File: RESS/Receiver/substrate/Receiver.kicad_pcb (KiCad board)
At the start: 2 copper layers, 94 x 71.1 mm, 19 parts, among them J3 ADP_L, J4 ADP_R, J5 Power, J6 RESS_OUT1, SW1 SW_SPDT, SW2 SW_DIP_x02, U1 LTV-817, U2 RR-1A, U3 TA48033S, U4 TC74HC32AP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

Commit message: P10を3.3Vと接続するのを忘れていたので修正
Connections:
- J4 pad 5: (no net) -> +3V3
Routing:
- net +3V3: track 55.6 -> 65.1 mm

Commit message: 送信基板の追加とファイルの整理
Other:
- board text added: "JLCJLCJLCJLC"

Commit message: 回路の細かな修正
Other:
- board text added: "RESS-Receiver 2022 Ichinoseki-B"
- board text removed: "RESS-Receiver 2022 Ichinoseki-B Falco"

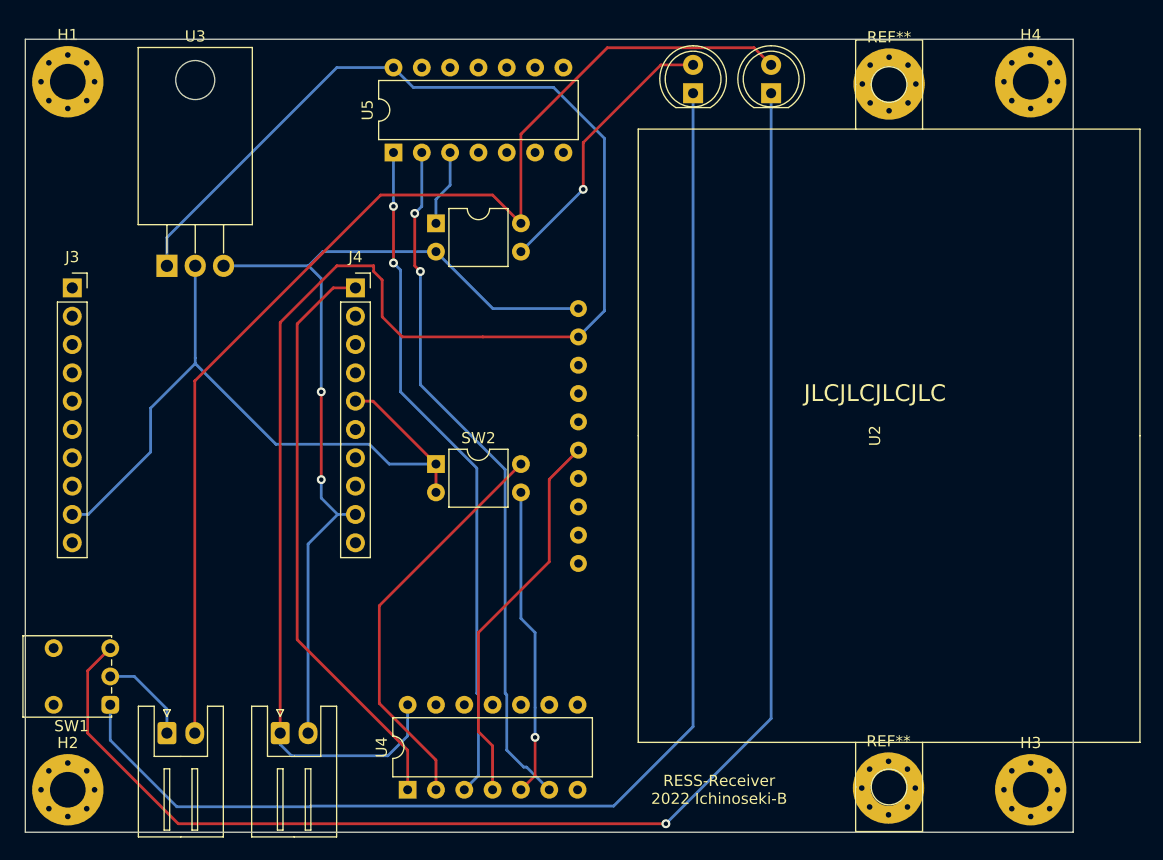
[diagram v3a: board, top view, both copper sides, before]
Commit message: 基板が燃えるほどのミスを修正
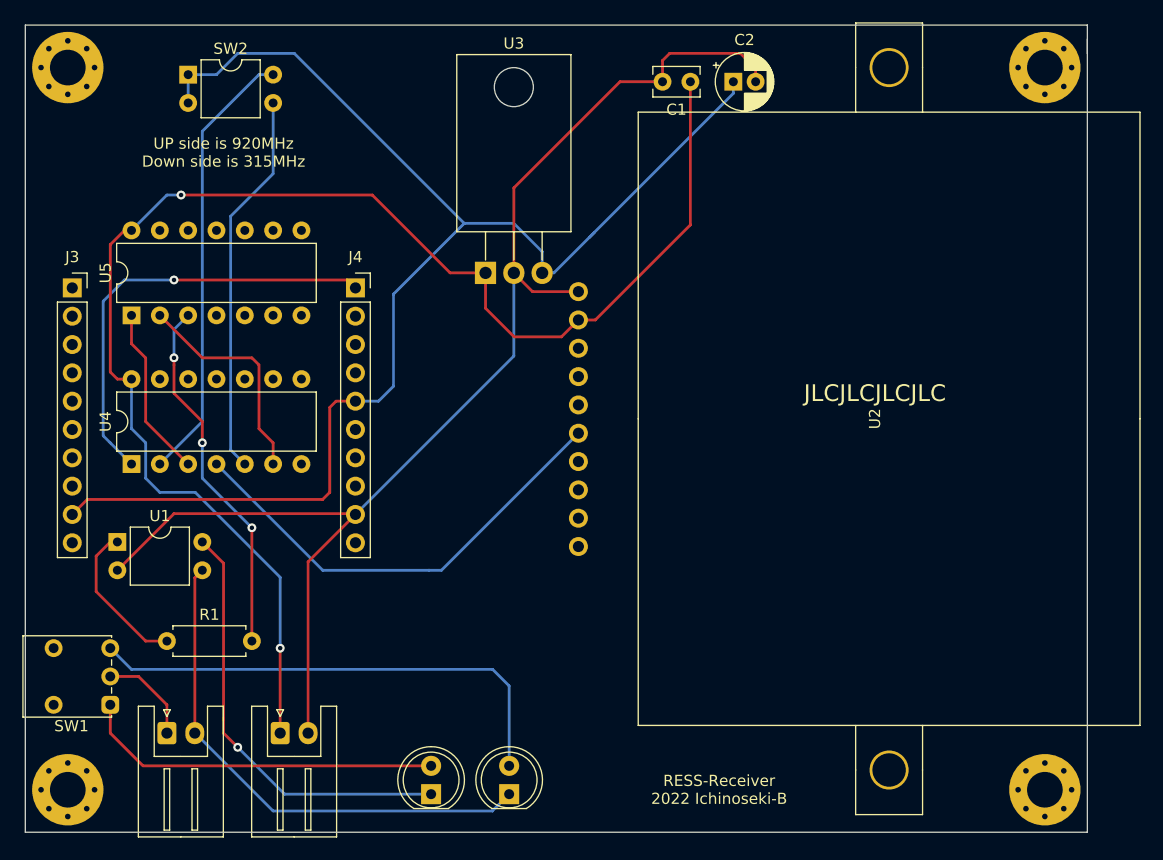
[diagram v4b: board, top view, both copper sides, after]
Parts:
- removed REF** (x2): MountingHole_3.2mm_M3_Pad_Via, MountingHole:MountingHole_3.2mm_M3_Pad_Via
- added C1: 0.33μF, Capacitor_THT:C_Rect_L4.0mm_W2.5mm_P2.50mm, F.Cu at (160.0, 85.1)
- added C2: 47μF, Capacitor_THT:CP_Radial_D5.0mm_P2.00mm, F.Cu at (163.8, 85.1)
- added R1: 220Ω, Resistor_THT:R_Axial_DIN0207_L6.3mm_D2.5mm_P7.62mm_Horizontal, F.Cu at (113.0, 135.3)
- U1: value LTV-817 -> TLP785
- U3: value TA48033S -> AP2204R-3.3
- moved D1 67.1 mm to (136.7, 149.0)
- moved D2 67.1 mm to (143.7, 149.0)
- moved SW2 41.4 mm to (114.9, 84.5)
- moved U1 40.4 mm to (108.6, 126.4)
- moved U4 38.3 mm to (109.9, 119.4)
- moved U3 28.6 mm to (141.6, 102.2)
- moved U5 27.7 mm to (109.9, 106.0)
- moved H4 1.80 mm to (191.8, 83.8)
- moved U2 1.52 mm to (177.8, 115.3)
- moved H1 1.27 mm to (104.1, 83.8)
- moved H3 1.27 mm to (191.8, 148.6)
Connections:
- J6 pad 2: Net-(D2-Pad2) -> Net-(D2-Pad1)
- SW1 pad 1: Net-(D1-Pad1) -> Net-(D1-Pad2)
- SW1 pad 3: Net-(D2-Pad1) -> Net-(D2-Pad2)
- U1 pad 1: OUT -> Net-(R1-Pad1)
- U1 pad 3: Net-(D1-Pad2) -> Net-(D2-Pad1)
- U1 pad 4: Net-(D2-Pad2) -> Net-(D1-Pad1)
- U3 pad 2: +3V3 -> GND
- U3 pad 3: GND -> +3V3
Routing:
- net Net-(D2-Pad1): track 133.1 -> 46.6 mm, vias 1 -> 0
- net Net-(D1-Pad1): track 117.7 -> 38.8 mm, vias 0 -> 1
- net +3V3: track 65.1 -> 125.1 mm
- net Net-(D2-Pad2): track 103.1 -> 44.3 mm
- net OUT5: track 60.8 -> 15.4 mm, vias 2 -> 0
- net OUT6: track 62.6 -> 20.1 mm, vias 2 -> 0
- net GND: track 80.2 -> 115.9 mm, vias 2 -> 0
- net OUT: track 6.88 -> 32.6 mm, vias 0 -> 3
- net +5V: track 156.4 -> 130.7 mm, vias 0 -> 2
- net Net-(R1-Pad1): track 0.00 -> 13.8 mm
- net OUT1: track 52.4 -> 40.0 mm, vias 0 -> 1
- net Net-(D1-Pad2): track 24.8 -> 32.5 mm, vias 1 -> 0
- net OUT2: track 34.7 -> 41.5 mm
- net OUT4: track 27.7 -> 34.5 mm, vias 1 -> 0
- net OUT3: track 36.6 -> 39.9 mm
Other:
- board size 94 x 71.1 mm -> 95.3 x 72.4 mm
- board text added: "UP side is 920MHz Down side is 315MHz"
